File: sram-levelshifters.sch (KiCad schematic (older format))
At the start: 7 parts, among them U5 ISSI61WV5128BL

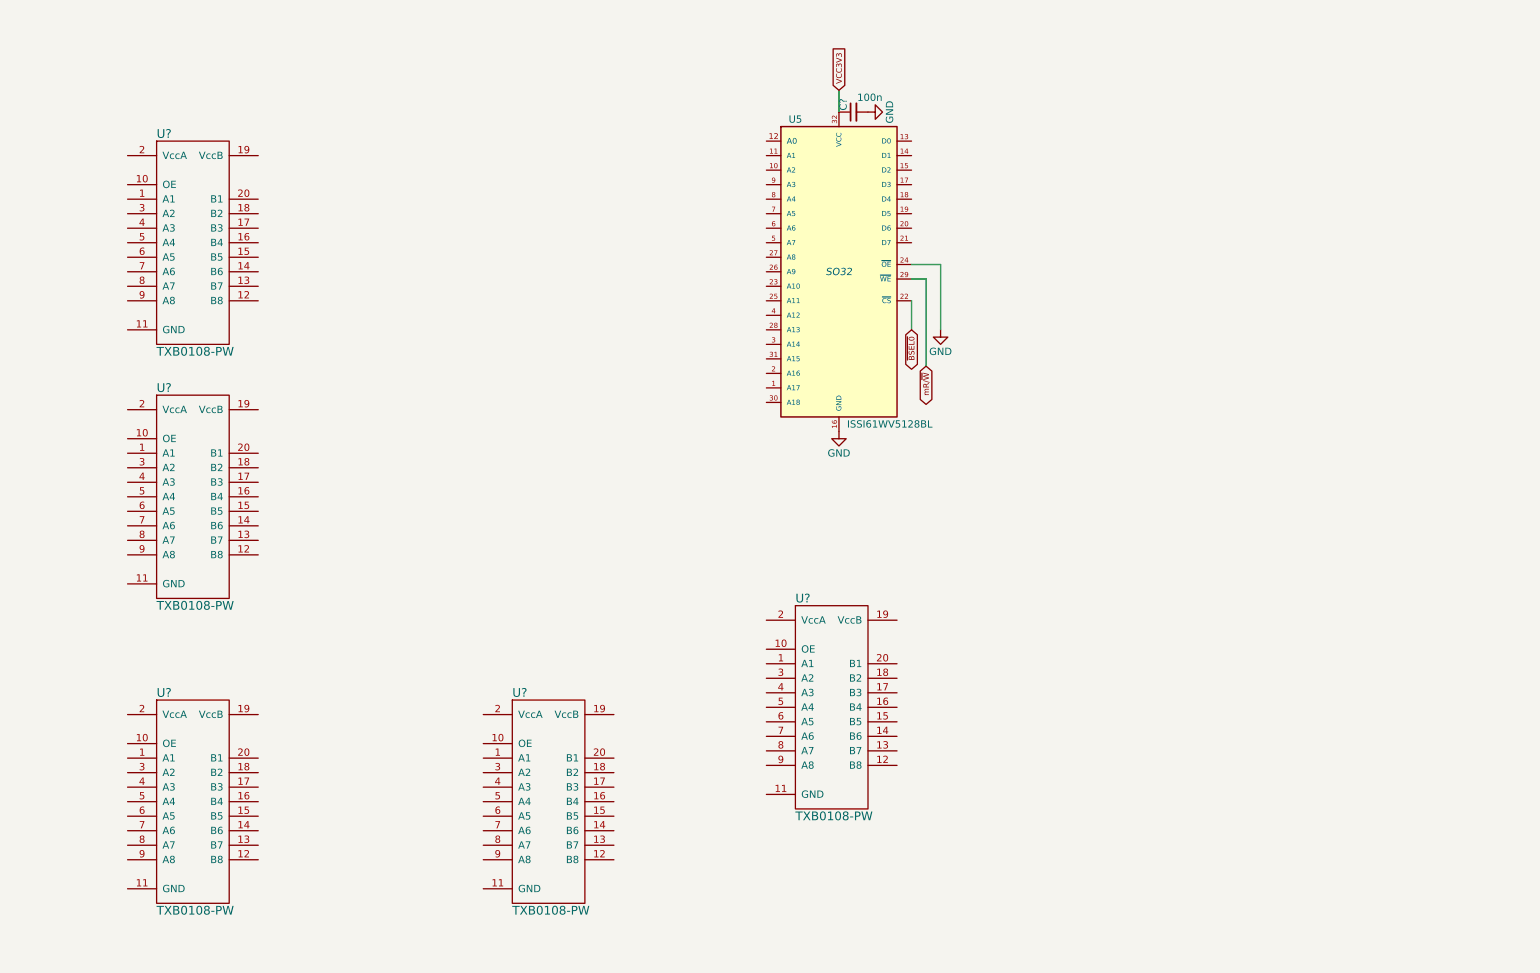
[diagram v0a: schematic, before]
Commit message: added some footprint and revised logic for address selection
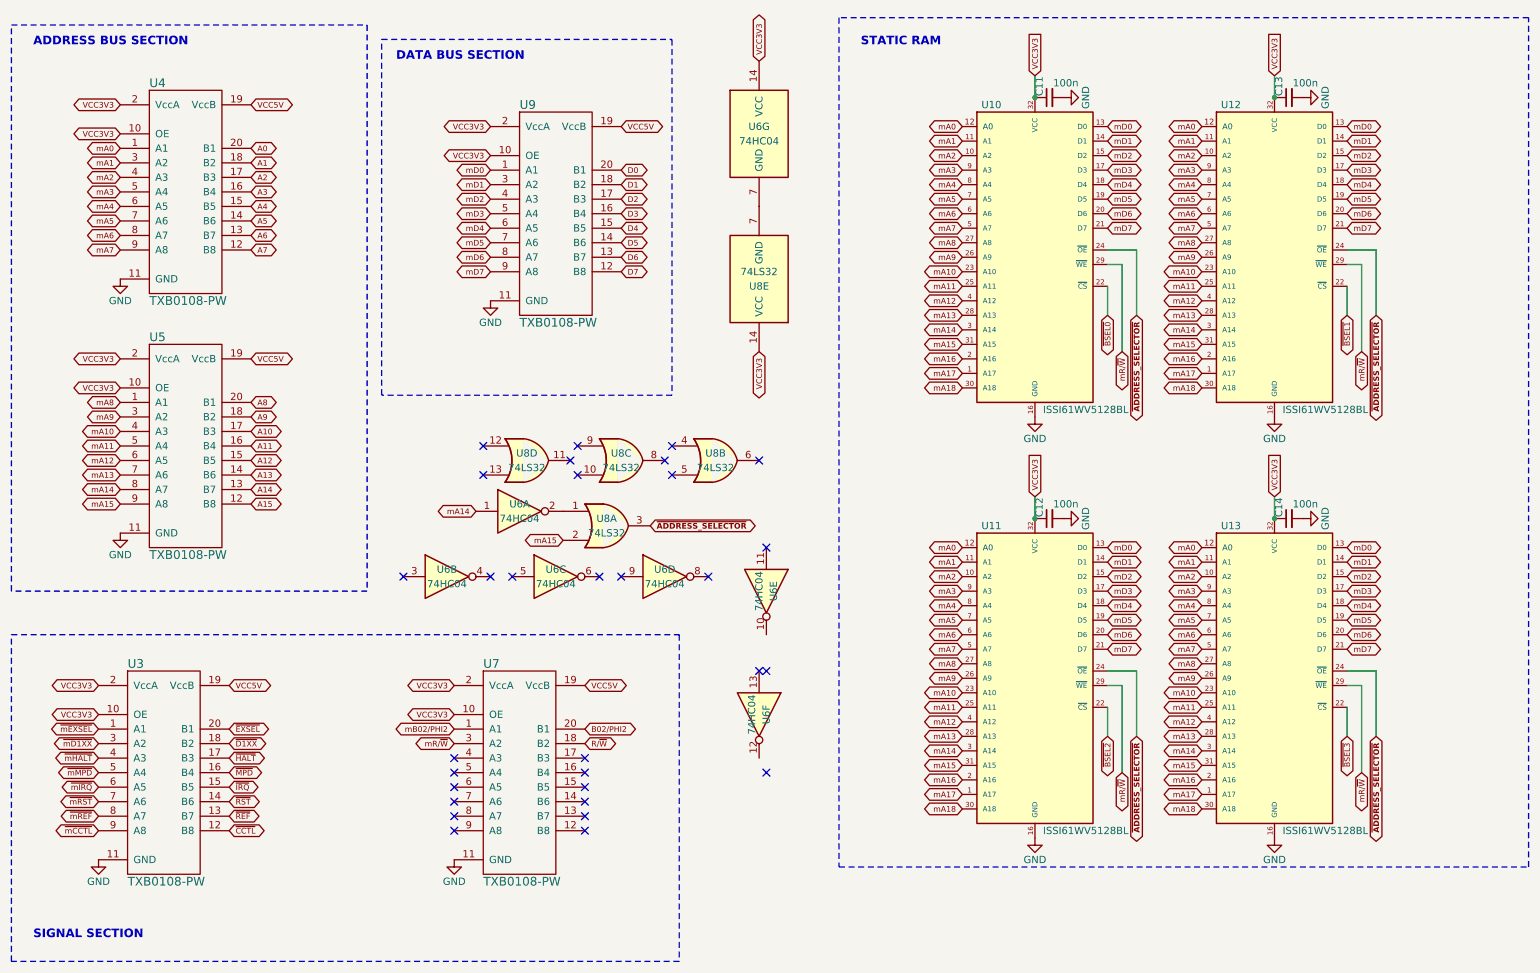
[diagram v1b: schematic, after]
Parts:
- added C12, C13, C14: 100n, Capacitors_SMD:C_1206_HandSoldering, symbol C_Small
- added U11, U12, U13: ISSI61WV5128BL, RetroBitLab:ISSI61-64WV5128Axx-Bxx-32, symbol ISSI61WV5128BL
- added U6: 74HC04, Housings_DIP:DIP-14_W7.62mm, symbol 74HC04
- added U8: 74LS32, Housings_DIP:DIP-14_W7.62mm, symbol 74LS32
- C11: renamed from C?; footprint (none) -> Capacitors_SMD:C_1206_HandSoldering
- U10: renamed from U5; footprint SO32 -> RetroBitLab:ISSI61-64WV5128Axx-Bxx-32
- U3, U4, U5, U7, U9: renamed from U?; footprint (none) -> Housings_SSOP:SSOP-20_4.4x6.5mm_Pitch0.65mm
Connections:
- net GND: now also U3.11 (GND), U4.11 (GND), U5.11 (GND), U7.11 (GND), U9.11 (GND), C12.2, C13.2, C14.2, U11.16 (GND), U12.16 (GND), U13.16 (GND); no longer U10.24 (~OE)
- net VCC3V3: now also U3.10 (OE), U3.2 (VccA), U4.10 (OE), U4.2 (VccA), U5.10 (OE), U5.2 (VccA), U7.10 (OE), U7.2 (VccA), U9.10 (OE), U9.2 (VccA), C12.1, C13.1, C14.1, U11.32 (VCC), U12.32 (VCC), U13.32 (VCC), U6.14 (VCC), U8.14 (VCC)
- net mR/~W: now also U7.3 (A2), U11.29 (~WE), U12.29 (~WE), U13.29 (~WE)
- net mA17: now reaches U10.1 (A17)
- net mA17: now also U11.1 (A17), U12.1 (A17), U13.1 (A17)
- net mA2: now reaches U10.10 (A2)
- net mA2: now also U4.4 (A3), U11.10 (A2), U12.10 (A2), U13.10 (A2)
- net mA1: now reaches U10.11 (A1)
- net mA1: now also U4.3 (A2), U11.11 (A1), U12.11 (A1), U13.11 (A1)
- net mA0: now reaches U10.12 (A0)
- net mA0: now also U4.1 (A1), U11.12 (A0), U12.12 (A0), U13.12 (A0)
- net mD0: now reaches U10.13 (D0)
- net mD0: now also U9.1 (A1), U11.13 (D0), U12.13 (D0), U13.13 (D0)
- net mD1: now reaches U10.14 (D1)
- net mD1: now also U9.3 (A2), U11.14 (D1), U12.14 (D1), U13.14 (D1)
- net mD2: now reaches U10.15 (D2)
- net mD2: now also U9.4 (A3), U11.15 (D2), U12.15 (D2), U13.15 (D2)
- net mD3: now reaches U10.17 (D3)
- net mD3: now also U9.5 (A4), U11.17 (D3), U12.17 (D3), U13.17 (D3)
- net mD4: now reaches U10.18 (D4)
- net mD4: now also U9.6 (A5), U11.18 (D4), U12.18 (D4), U13.18 (D4)
- net mD5: now reaches U10.19 (D5)
- net mD5: now also U9.7 (A6), U11.19 (D5), U12.19 (D5), U13.19 (D5)
- net mA16: now reaches U10.2 (A16)
- net mA16: now also U11.2 (A16), U12.2 (A16), U13.2 (A16)
- net mD6: now reaches U10.20 (D6)
- net mD6: now also U9.8 (A7), U11.20 (D6), U12.20 (D6), U13.20 (D6)
- net mD7: now reaches U10.21 (D7)
- net mD7: now also U9.9 (A8), U11.21 (D7), U12.21 (D7), U13.21 (D7)
- net mA10: now reaches U10.23 (A10)
- net mA10: now also U5.4 (A3), U11.23 (A10), U12.23 (A10), U13.23 (A10)
- net mA11: now reaches U10.25 (A11)
- net mA11: now also U5.5 (A4), U11.25 (A11), U12.25 (A11), U13.25 (A11)
- net mA9: now reaches U10.26 (A9)
- net mA9: now also U5.3 (A2), U11.26 (A9), U12.26 (A9), U13.26 (A9)
- net mA8: now reaches U10.27 (A8)
- net mA8: now also U5.1 (A1), U11.27 (A8), U12.27 (A8), U13.27 (A8)
- net mA13: now reaches U10.28 (A13)
- net mA13: now also U5.7 (A6), U11.28 (A13), U12.28 (A13), U13.28 (A13)
- net mA14: now reaches U10.3 (A14)
- net mA14: now also U5.8 (A7), U11.3 (A14), U12.3 (A14), U13.3 (A14), U6.1
- net mA18: now reaches U10.30 (A18)
- net mA18: now also U11.30 (A18), U12.30 (A18), U13.30 (A18)
- net mA15: now reaches U10.31 (A15)
- net mA15: now also U5.9 (A8), U11.31 (A15), U12.31 (A15), U13.31 (A15), U8.2
- net mA12: now reaches U10.4 (A12)
- net mA12: now also U5.6 (A5), U11.4 (A12), U12.4 (A12), U13.4 (A12)
- net mA7: now reaches U10.5 (A7)
- net mA7: now also U4.9 (A8), U11.5 (A7), U12.5 (A7), U13.5 (A7)
- net mA6: now reaches U10.6 (A6)
- net mA6: now also U4.8 (A7), U11.6 (A6), U12.6 (A6), U13.6 (A6)
- net mA5: now reaches U10.7 (A5)
- net mA5: now also U4.7 (A6), U11.7 (A5), U12.7 (A5), U13.7 (A5)
- net mA4: now reaches U10.8 (A4)
- net mA4: now also U4.6 (A5), U11.8 (A4), U12.8 (A4), U13.8 (A4)
- net mA3: now reaches U10.9 (A3)
- net mA3: now also U4.5 (A4), U11.9 (A3), U12.9 (A3), U13.9 (A3)
- net A15: now reaches U5.12 (B8)
- net A14: now reaches U5.13 (B7)
- net A13: now reaches U5.14 (B6)
- net A12: now reaches U5.15 (B5)
- net A11: now reaches U5.16 (B4)
- net A10: now reaches U5.17 (B3)
- net A9: now reaches U5.18 (B2)
- net VCC5V: now reaches U5.19 (VccB)
- net VCC5V: now also U3.19 (VccB), U4.19 (VccB), U7.19 (VccB), U9.19 (VccB)
- net A8: now reaches U5.20 (B1)
- net A7: now reaches U4.12 (B8)
- net A6: now reaches U4.13 (B7)
- net A5: now reaches U4.14 (B6)
- net A4: now reaches U4.15 (B5)
- net A3: now reaches U4.16 (B4)
- net A2: now reaches U4.17 (B3)
- net A1: now reaches U4.18 (B2)
- net A0: now reaches U4.20 (B1)
- net ~mEXSEL: now reaches U3.1 (A1)
- net ~CCTL: now reaches U3.12 (B8)
- net ~REF: now reaches U3.13 (B7)
- net ~RST: now reaches U3.14 (B6)
- net ~IRQ: now reaches U3.15 (B5)
- net ~MPD: now reaches U3.16 (B4)
- net ~HALT: now reaches U3.17 (B3)
- net ~D1XX: now reaches U3.18 (B2)
- net ~EXSEL: now reaches U3.20 (B1)
- net ~mD1XX: now reaches U3.3 (A2)
- net ~mHALT: now reaches U3.4 (A3)
- net ~mMPD: now reaches U3.5 (A4)
- net ~mIRQ: now reaches U3.6 (A5)
- net ~mRST: now reaches U3.7 (A6)
- net ~mREF: now reaches U3.8 (A7)
- net ~mCCTL: now reaches U3.9 (A8)
- net mB02/PHI2: now reaches U7.1 (A1)
- net R/~W: now reaches U7.18 (B2)
- net B02/PHI2: now reaches U7.20 (B1)
- net D7: now reaches U9.12 (B8)
- net D6: now reaches U9.13 (B7)
- net D5: now reaches U9.14 (B6)
- net D4: now reaches U9.15 (B5)
- net D3: now reaches U9.16 (B4)
- net D2: now reaches U9.17 (B3)
- net D1: now reaches U9.18 (B2)
- net D0: now reaches U9.20 (B1)
- new net: U6.2, U8.1
- new net: U6.7 (GND), U8.7 (GND)
- new net ~ADDRESS_SELECTOR: U10.24 (~OE), U11.24 (~OE), U12.24 (~OE), U13.24 (~OE), U8.3
- new net ~BSEL1: U12.22 (~CS)
- new net ~BSEL2: U11.22 (~CS)
- new net ~BSEL3: U13.22 (~CS)
- no-connect marks 0 -> 31
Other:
- note added: "ADDRESS BUS SECTION"
- note added: "DATA BUS SECTION"
- note added: "SIGNAL SECTION"
- note added: "STATIC RAM"
- moved on the sheet: C11, U10, U3, U4, U5, U7, U9

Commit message: modified logic & added pcb
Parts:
- U11: renamed from U10; footprint RetroBitLab:ISSI61-64WV5128Axx-Bxx-32 -> RetroBitLab:SOP-32L-20.5x11.30-1.27mm
- U12: renamed from U11; footprint RetroBitLab:ISSI61-64WV5128Axx-Bxx-32 -> RetroBitLab:SOP-32L-20.5x11.30-1.27mm
- U13: renamed from U12; footprint RetroBitLab:ISSI61-64WV5128Axx-Bxx-32 -> RetroBitLab:SOP-32L-20.5x11.30-1.27mm
- U14: renamed from U13; footprint RetroBitLab:ISSI61-64WV5128Axx-Bxx-32 -> RetroBitLab:SOP-32L-20.5x11.30-1.27mm
- U7: renamed from U6; footprint Housings_DIP:DIP-14_W7.62mm -> Housings_SSOP:TSSOP-14_4.4x5mm_Pitch0.65mm
- U9: renamed from U8; footprint Housings_DIP:DIP-14_W7.62mm -> Housings_SSOP:SSOP-14_5.3x6.2mm_Pitch0.65mm
- renumbered C11 to C10, C12 to C11, C13 to C12, C14 to C13, U9 to U10, U3 to U4, U4 to U5, U5 to U6, U7 to U8
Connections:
- net GND: now also U7.7 (GND), U9.7 (GND)
- net mA14: no longer U11.3 (A14), U12.3 (A14), U13.3 (A14), U14.3 (A14)
- net mA15: no longer U11.31 (A15), U12.31 (A15), U13.31 (A15), U14.31 (A15)
- net mA16 renamed PB2
- net mA17 renamed PB3
- net mA18 renamed PB4
- new net PB0: U11.3 (A14), U12.3 (A14), U13.3 (A14), U14.3 (A14)
- new net PB1: U11.31 (A15), U12.31 (A15), U13.31 (A15), U14.31 (A15)
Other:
- moved on the sheet: C10, C11, C12, C13, U10
